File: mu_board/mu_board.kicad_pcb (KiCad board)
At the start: 2 copper layers, 23.1 x 33 mm, 32 parts, among them J1 USB_C_Receptacle, J2 Conn_01x11, J3 Conn_01x08, J4 Conn_01x13, J5 Conn_01x06, U1 MIC5216-3.3BM5, U2 ATXMEGA-A4U-EPAD, U3 nRF24L01_module

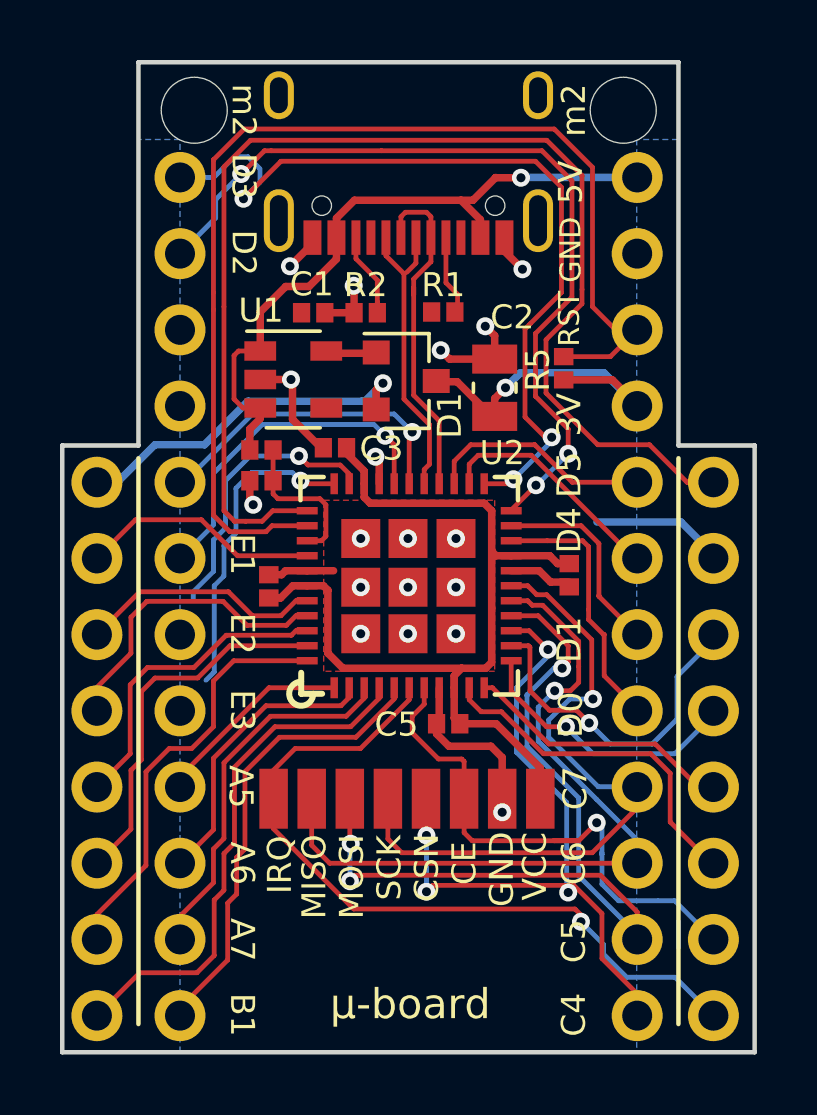
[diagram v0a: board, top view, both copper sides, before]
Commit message: minor PCB fixes and BOM updates
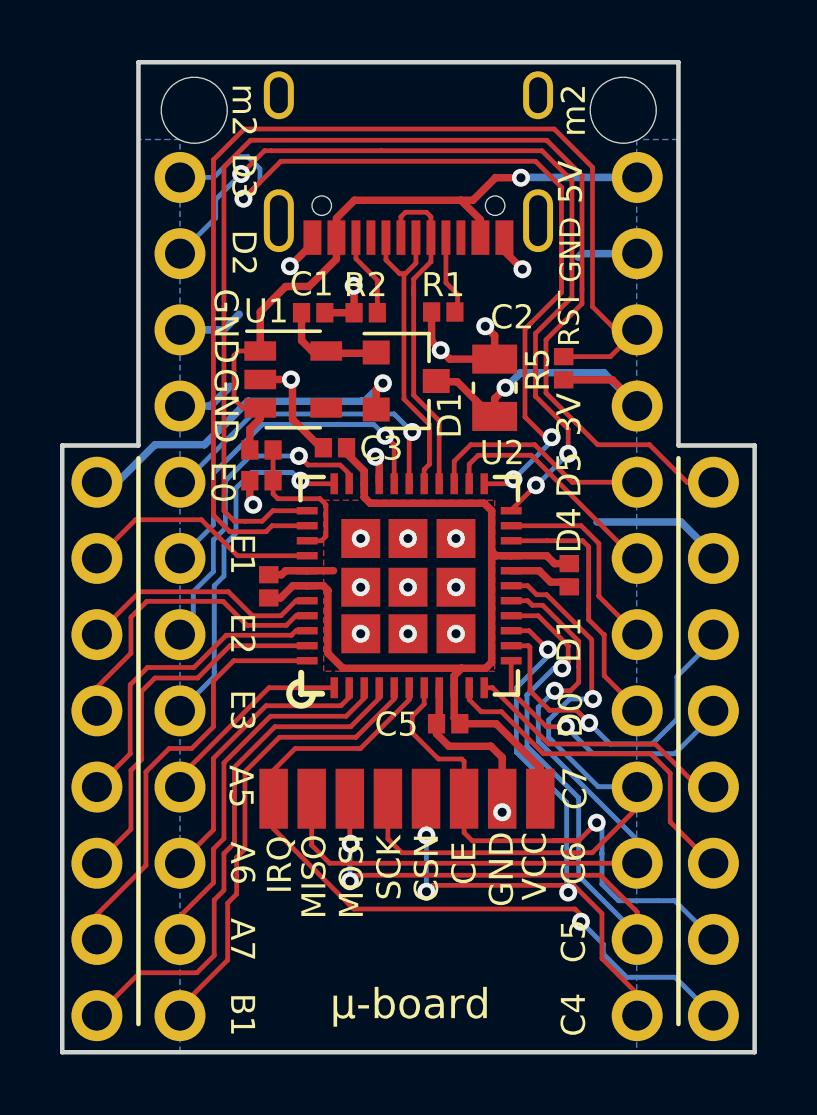
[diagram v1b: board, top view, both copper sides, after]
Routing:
- net GND: track 28.2 -> 35.8 mm
- net Net-(C1-Pad2): track 1.50 -> 3.39 mm
- net /PE3: track 10.5 -> 11.8 mm
- net /PE2: track 9.49 -> 10.8 mm
